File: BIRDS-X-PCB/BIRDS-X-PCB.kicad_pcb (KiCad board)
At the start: 2 copper layers, 85 x 85 mm, 84 parts, among them J101 LPC-50M2LG, J102 Conn_02x04_Odd_Even, J201 Conn_01x02, J202 Conn_01x02, J203 Conn_01x02, J401 Conn_01x04, J402 Conn_01x08, J403 Conn_01x02, J404 MHDR2X5, Q201 SI1470DH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

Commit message: PCB updated
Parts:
- moved U307 48.3 mm to (95.2, 97.5)
- moved R301 47.1 mm to (101.0, 97.0), turned to 90 degrees
- moved TP301 35.6 mm to (56.2, 68.0)
- moved JP301 19.5 mm to (87.0, 53.8)
- moved TP401 4.51 mm to (56.2, 72.0)
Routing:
- net Net-(U304-DIODE_ANODE): track 0.00 -> 103.8 mm
- net BOOT0: track 6.35 -> 103.2 mm, vias 0 -> 8
- net UART_TX_JASPER_TO_BOSS: track 0.00 -> 86.3 mm, vias 0 -> 2
- net TEMP_SENSE_1: track 0.00 -> 82.5 mm, vias 0 -> 4
- net ST_SWDIO: track 0.00 -> 82.5 mm, vias 0 -> 7
- net UART_RX_BOSS_TO_JASPER: track 0.00 -> 80.8 mm, vias 0 -> 2
- net Net-(U303-DIODE_ANODE): track 0.00 -> 77.6 mm, vias 0 -> 3
- net ST_RST: track 16.1 -> 86.3 mm, vias 2 -> 5
- net Net-(U301-DIODE_ANODE): track 0.00 -> 52.0 mm, vias 0 -> 2
- net DIO1_3V3_EN_FROM_BOSS: track 3.49 -> 50.0 mm, vias 0 -> 3
- net Net-(D301-K): track 0.00 -> 44.8 mm, vias 0 -> 3
- net Net-(U401-PA11/PA9): track 0.00 -> 41.4 mm, vias 0 -> 2
- net Net-(U302-DIODE_ANODE): track 0.00 -> 39.0 mm, vias 0 -> 2
- net SUP_3V3_2: track 7.48 -> 45.9 mm, vias 0 -> 1
- net Net-(JP301-B): track 0.00 -> 34.0 mm, vias 0 -> 2
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
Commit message: Fix DRC issues
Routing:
- net Net-(J402-Pin_7): track 5.62 -> 46.4 mm, vias 0 -> 4
- net GND: track 2.54 -> 26.9 mm, vias 0 -> 24
- net Net-(J402-Pin_3): track 4.12 -> 23.7 mm, vias 0 -> 3
- net ST_RST: track 86.3 -> 90.5 mm, vias 5 -> 6
- net Net-(U305A--): track 0.00 -> 3.31 mm
- net Net-(U305B--): track 0.00 -> 3.25 mm
- net Net-(U302-DIODE_ANODE): track 39.0 -> 36.0 mm
- net SUP_UNREG_2: track 0.00 -> 2.00 mm
- net SUP_3V3_1: track 0.00 -> 2.00 mm
- net BOOT0: track 103.2 -> 101.4 mm, vias 8 -> 6
- net SUP_5V0: track 33.3 -> 31.8 mm
- net RFET_EN3: track 76.3 -> 74.9 mm, vias 5 -> 4
- net SUP_3V3_2: track 45.9 -> 44.8 mm
- net DIO1_3V3_EN_FROM_BOSS: track 50.0 -> 48.9 mm
- net +5V: track 82.6 -> 81.7 mm
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
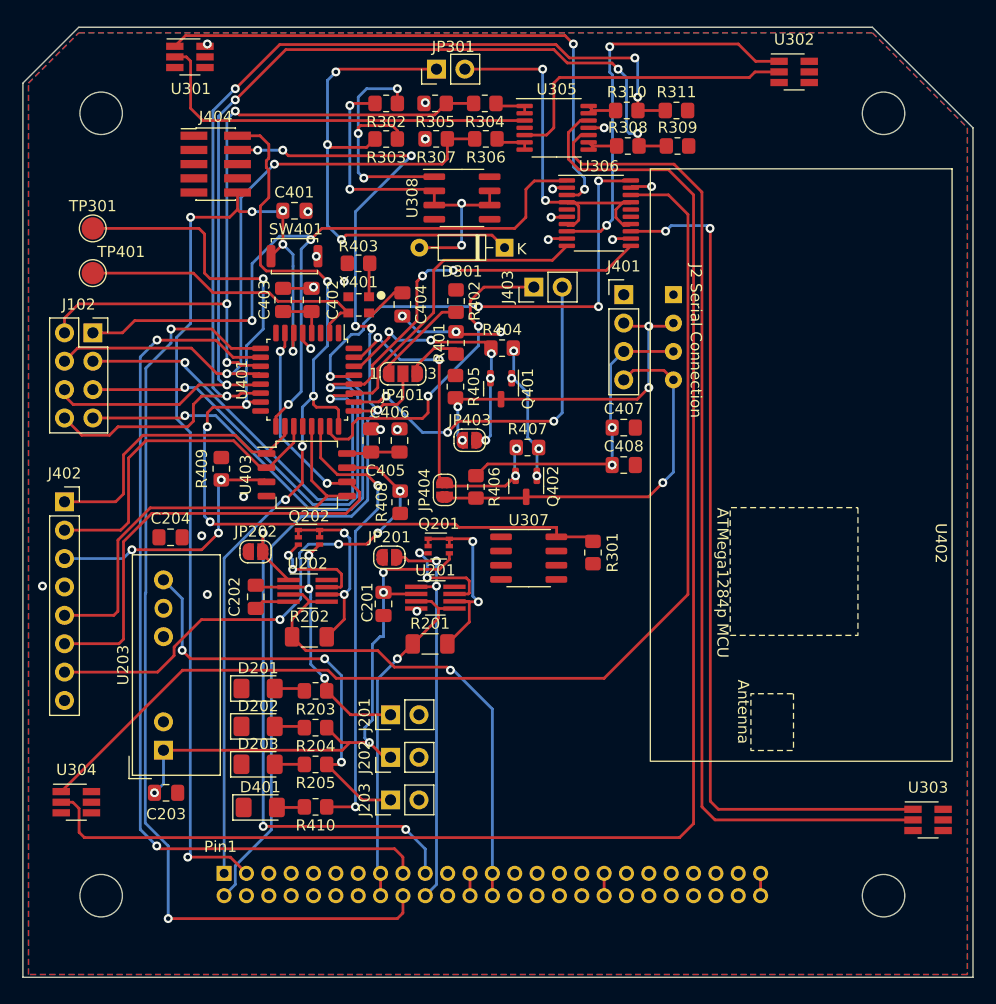
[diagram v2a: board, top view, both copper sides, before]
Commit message: Finish fixing DRC issues, except power lines
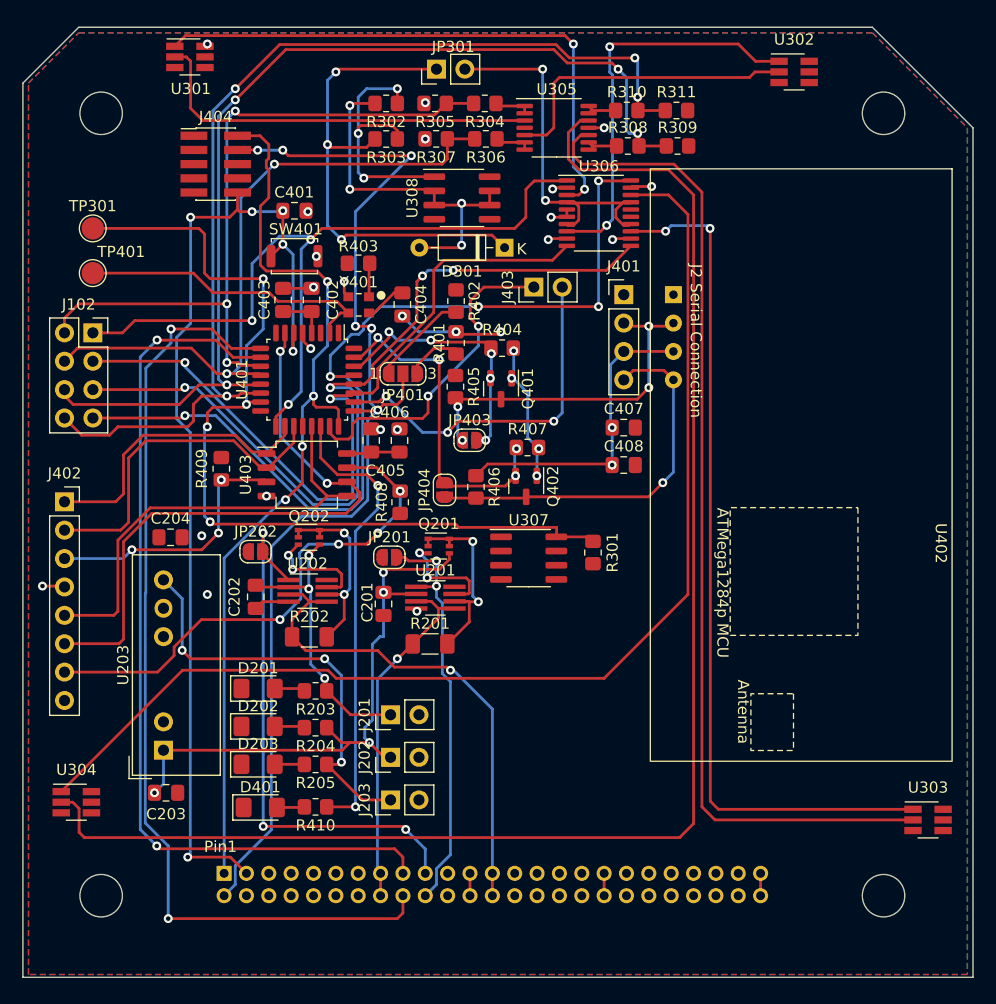
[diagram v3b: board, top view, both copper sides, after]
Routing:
- net GND: track 26.9 -> 31.0 mm
- net DIO2_5V_EN_FROM_BOSS: track 35.9 -> 36.9 mm
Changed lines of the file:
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@@
       (net 20 "SUP_5V0") (pinfunction "GATEP") (pintype "output"))
     (pad "4" smd rect (at -1.71 0.97) (size 2 0.4) (layers "F.Cu" "F.Paste" "F.Mask")
-      (net 2 "GND") (pinfunction "GND") (pintype "power_in"))
+      (net 2 "GND") (pinfunction "GND") (pintype "power_in") (zone_connect 2))
     (pad "5" smd rect (at 1.71 0.97) (size 2 0.4) (layers "F.Cu" "F.Paste" "F.Mask")
       (net 20 "SUP_5V0") (pinfunction "IN") (pintype "input"))
@@
       (net 28 "SUP_3V3_2") (pinfunction "GATEP") (pintype "output"))
     (pad "4" smd rect (at -1.71 0.97) (size 2 0.4) (layers "F.Cu" "F.Paste" "F.Mask")
-      (net 2 "GND") (pinfunction "GND") (pintype "power_in"))
+      (net 2 "GND") (pinfunction "GND") (pintype "power_in") (zone_connect 2))
     (pad "5" smd rect (at 1.71 0.97) (size 2 0.4) (layers "F.Cu" "F.Paste" "F.Mask")
       (net 28 "SUP_3V3_2") (pinfunction "IN") (pintype "input"))
@@
       (net 2 "GND") (pinfunction "GND") (pintype "power_in"))
     (pad "5" thru_hole oval (at 10.16 0 90) (size 1.7 1.7) (drill 1) (layers "*.Cu" "*.Mask")
-      (net 2 "GND") (pinfunction "0V/-Vo") (pintype "power_out"))
+      (net 2 "GND") (pinfunction "0V/-Vo") (pintype "power_out") (zone_connect 2))
     (pad "6" thru_hole oval (at 12.7 0 90) (size 1.7 1.6) (drill 1) (layers "*.Cu" "*.Mask")
       (net 83 "unconnected-(U203-NC{slash}0V-Pad6)") (pinfunction "NC/0V") (pintype "power_out+no_connect"))
@@
       (net 4 "+12V") (pinfunction "Pin_1") (pintype "passive"))
     (pad "2" thru_hole oval (at 0 2.54 90) (size 1.7 1.7) (drill 1) (layers "*.Cu" "*.Mask")
-      (net 2 "GND") (pinfunction "Pin_2") (pintype "passive"))
+      (net 2 "GND") (pinfunction "Pin_2") (pintype "passive") (zone_connect 2))
     (model "${KICAD6_3DMODEL_DIR}/Connector_PinHeader_2.54mm.3dshapes/PinHeader_1x02_P2.54mm_Vertical.wrl"
       (offset (xyz 0 0 0))
@@
       (net 126 "Net-(JP301-B)") (pintype "passive"))
     (pad "5" smd roundrect (at -2.8625 -0.325) (size 1.475 0.4) (layers "F.Cu" "F.Paste" "F.Mask") (roundrect_rratio 0.25)
-      (net 2 "GND") (pinfunction "VSS") (pintype "power_in"))
+      (net 2 "GND") (pinfunction "VSS") (pintype "power_in") (zone_connect 2))
     (pad "6" smd roundrect (at -2.8625 0.325) (size 1.475 0.4) (layers "F.Cu" "F.Paste" "F.Mask") (roundrect_rratio 0.25)
       (net 2 "GND") (pinfunction "GND") (pintype "power_in"))
@@
       (net 19 "unconnected-(J101-Pin_12-Pad12)") (pinfunction "Pin_12") (pintype "passive+no_connect"))
     (pad "13" thru_hole oval locked (at 0 -12 270) (size 1.35 1.35) (drill 0.8) (layers "*.Cu" "*.Mask")
-      (net 2 "GND") (pinfunction "Pin_13") (pintype "passive"))
+      (net 2 "GND") (pinfunction "Pin_13") (pintype "passive") (zone_connect 2))
     (pad "14" thru_hole oval locked (at 2 -12 270) (size 1.35 1.35) (drill 0.8) (layers "*.Cu" "*.Mask")
-      (net 2 "GND") (pinfunction "Pin_14") (pintype "passive"))
+      (net 2 "GND") (pinfunction "Pin_14") (pintype "passive") (zone_connect 2))
     (pad "15" thru_hole oval locked (at 0 -14 270) (size 1.35 1.35) (drill 0.8) (layers "*.Cu" "*.Mask")
       (net 20 "SUP_5V0") (pinfunction "Pin_15") (pintype "passive"))
@@
   (segment (start 81.949695 104.525) (end 82.26 104.525) (width 0.25) (layer "B.Cu") (net 1))
   (segment (start 62.575 117.69) (end 61.77 118.495) (width 0.25) (layer "B.Cu") (net 1))
+  (segment (start 78.75 72.75) (end 78.75 73.744) (width 0.25) (layer "F.Cu") (net 2))
+  (segment (start 51.75 100) (end 53.645 100) (width 0.25) (layer "F.Cu") (net 2))
   (segment (start 88.975 77.475) (end 88.75 77.25) (width 0.25) (layer "F.Cu") (net 2))
+  (segment (start 78.75 73.744) (end 79.121 74.115) (width 0.25) (layer "F.Cu") (net 2))
   (segment (start 75.932 73.363) (end 75.819 73.363) (width 0.25) (layer "F.Cu") (net 2))
   (segment (start 97.09 68.91) (end 97 69) (width 0.25) (layer "F.Cu") (net 2))
@@
   (segment (start 92.75 77.25) (end 92.525 77.475) (width 0.25) (layer "F.Cu") (net 2))
   (segment (start 97.25 67) (end 98.625 67) (width 0.25) (layer "F.Cu") (net 2))
+  (segment (start 53.645 100) (end 53.721 100.076) (width 0.25) (layer "F.Cu") (net 2))
   (segment (start 106.25 64.25) (end 104.5 64.25) (width 0.25) (layer "F.Cu") (net 2))
   (segment (start 97.5045 64.36) (end 98.665 64.36) (width 0.25) (layer "F.Cu") (net 2))
@@
   (segment (start 71.435 101.395) (end 73.76 101.395) (width 0.25) (layer "F.Cu") (net 2))
   (segment (start 102.84 68.91) (end 102.75 69) (width 0.25) (layer "F.Cu") (net 2))
+  (segment (start 98.665 66.31) (end 98.665 66.96) (width 0.25) (layer "F.Cu") (net 2))
   (segment (start 70.83 102) (end 71.435 101.395) (width 0.25) (layer "F.Cu") (net 2))
   (segment (start 102 59) (end 100.6125 59) (width 0.25) (layer "F.Cu") (net 2))
@@
   (via (at 88.75 77.25) (size 0.8) (drill 0.4) (layers "F.Cu" "B.Cu") (net 2))
   (via (at 76 73.25) (size 0.8) (drill 0.4) (layers "F.Cu" "B.Cu") (net 2))
-  (via (at 69.75 92) (size 0.8) (drill 0.4) (layers "F.Cu" "B.Cu") (free) (net 2))
+  (via (at 71.794 91.948) (size 0.8) (drill 0.4) (layers "F.Cu" "B.Cu") (free) (net 2))
   (via (at 97.39 64.4745) (size 0.8) (drill 0.4) (layers "F.Cu" "B.Cu") (free) (net 2))
   (via (at 83.947 75.8405) (size 0.8) (drill 0.4) (layers "F.Cu" "B.Cu") (net 2))
@@
   (via (at 87 97.75) (size 0.8) (drill 0.4) (layers "F.Cu" "B.Cu") (net 24))
   (via (at 87 100) (size 0.8) (drill 0.4) (layers "F.Cu" "B.Cu") (net 24))
-  (segment (start 87 100) (end 87 126.7) (width 0.25) (layer "B.Cu") (net 24))
-  (segment (start 87 126.7) (end 86 127.7) (width 0.25) (layer "B.Cu") (net 24))
+  (segment (start 87.525 107.825805) (end 88.25 108.550805) (width 0.25) (layer "B.Cu") (net 24))
+  (segment (start 87 101) (end 87.525 101.525) (width 0.25) (layer "B.Cu") (net 24))
+  (segment (start 87 125.285786) (end 87 126.7) (width 0.25) (layer "B.Cu") (net 24))
+  (segment (start 87.525 101.525) (end 87.525 107.825805) (width 0.25) (layer "B.Cu") (net 24))
+  (segment (start 88.25 108.550805) (end 88.25 124.035786) (width 0.25) (layer "B.Cu") (net 24))
+  (segment (start 87 100) (end 87 101) (width 0.25) (layer "B.Cu") (net 24))
   (segment (start 87 97.75) (end 87 100) (width 0.25) (layer "B.Cu") (net 24))
+  (segment (start 87 126.7) (end 86 127.7) (width 0.25) (layer "B.Cu") (net 24))
+  (segment (start 88.25 124.035786) (end 87 125.285786) (width 0.25) (layer "B.Cu") (net 24))
   (segment (start 90 127.7) (end 90 125.7) (width 0.25) (layer "F.Cu") (net 27))
   (segment (start 88.25 107.5255) (end 87.9745 107.25) (width 0.25) (layer "F.Cu") (net 28))

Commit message: Route power lines on 2-layer board, if desired
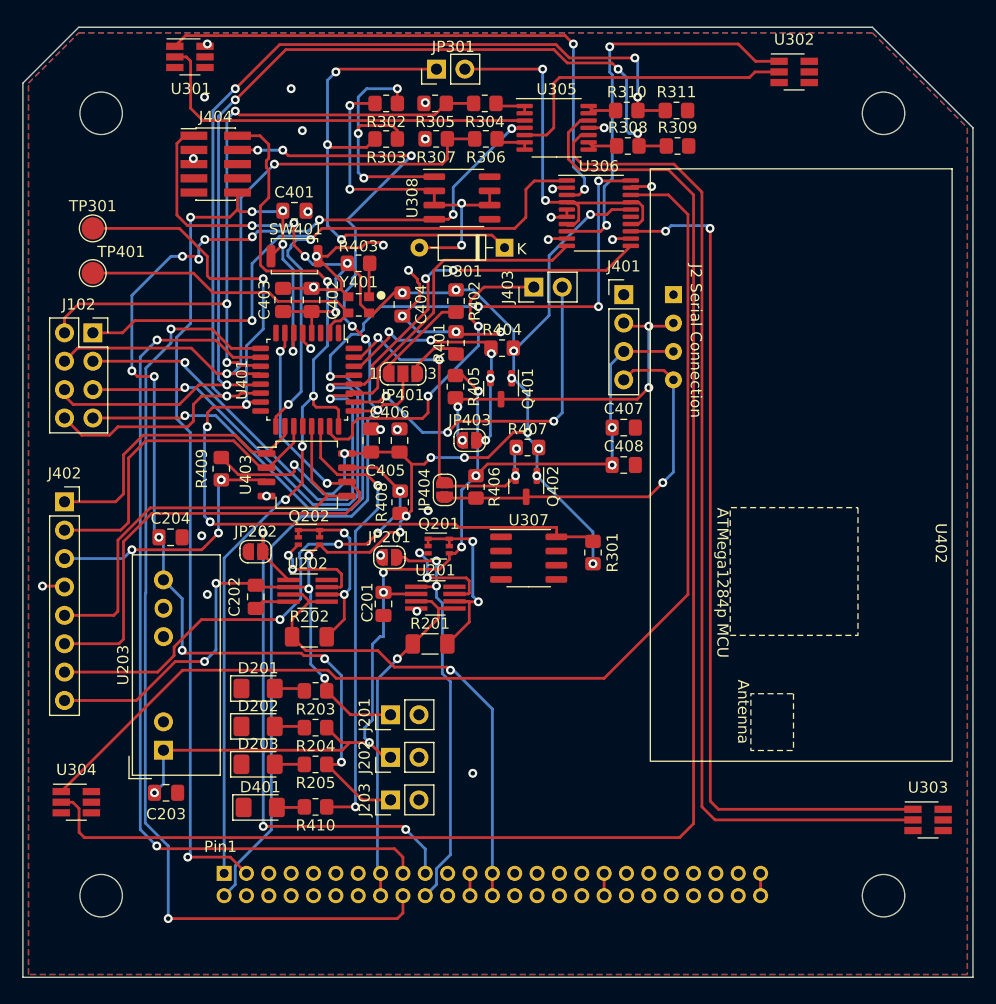
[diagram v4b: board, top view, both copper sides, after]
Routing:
- net +3V3: track 51.2 -> 201.8 mm, vias 7 -> 25
- net +12V: track 38.4 -> 109.6 mm, vias 3 -> 13
- net +5V: track 81.7 -> 100.2 mm, vias 6 -> 9
- net GND: track 31.0 -> 48.5 mm, vias 24 -> 32
- net RFET_EN1: track 70.7 -> 72.5 mm
- net TEMP_SENSE_1: track 81.8 -> 80.7 mm
- net BOOT0: track 101.4 -> 102.0 mm

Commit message: Minor layout changes to consolodate ground planes
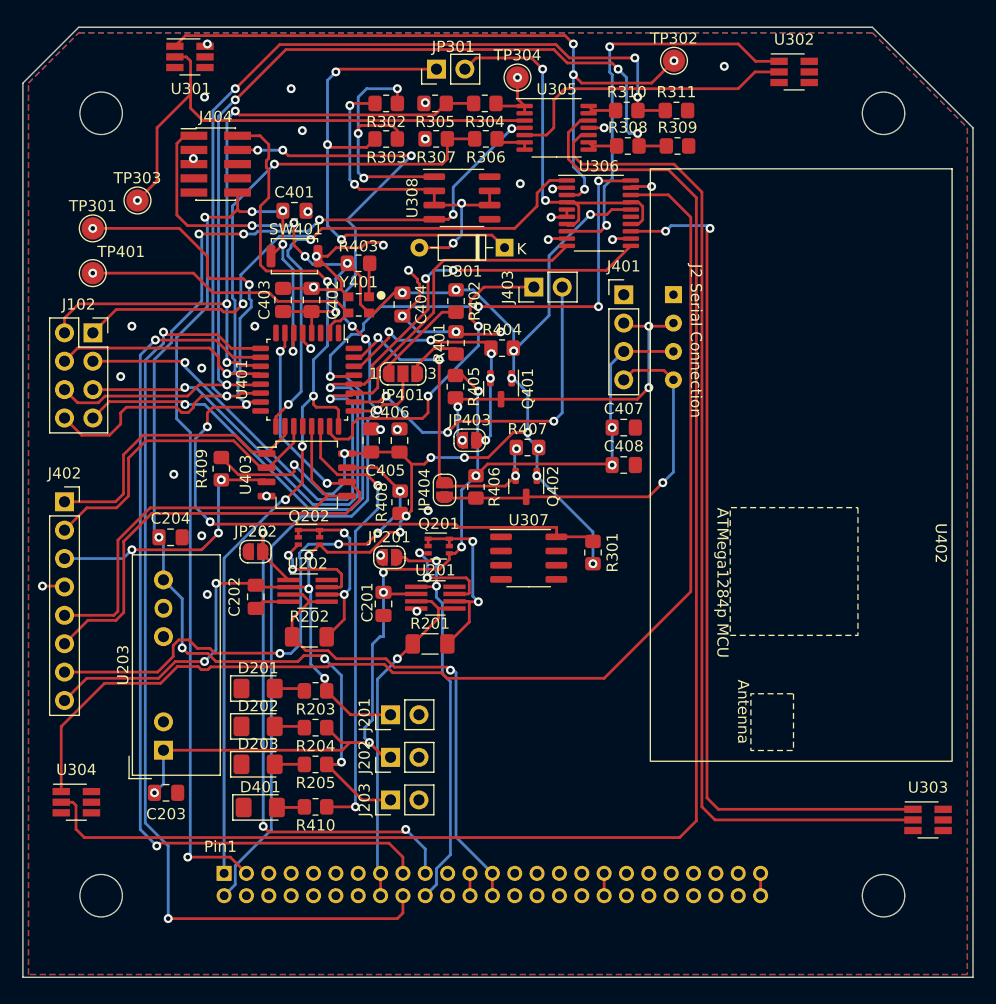
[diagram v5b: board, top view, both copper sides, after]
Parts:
- added TP302: TestPoint, TestPoint:TestPoint_Pad_D2.0mm, F.Cu at (108.2, 53.0)
- added TP303: TestPoint, TestPoint:TestPoint_Pad_D2.0mm, F.Cu at (60.2, 65.5)
- added TP304: TestPoint, TestPoint:TestPoint_Pad_D2.0mm, F.Cu at (94.2, 54.5)
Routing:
- net Net-(U301-SOURCE_BULK): track 36.1 -> 47.6 mm, vias 0 -> 1
- net Net-(U301-DIODE_ANODE): track 51.6 -> 61.7 mm, vias 2 -> 4
- net Net-(U304-DIODE_ANODE): track 103.8 -> 108.1 mm
- net Net-(J402-Pin_7): track 46.4 -> 49.9 mm
- net +12V: track 109.6 -> 106.3 mm, vias 13 -> 9
- net Net-(U305A--): track 3.31 -> 6.12 mm, vias 0 -> 1
- net RFET_EN1: track 72.5 -> 70.7 mm
- net MEM_MISO: track 30.6 -> 29.2 mm
- net MEM_CLK: track 56.2 -> 54.9 mm
- net Net-(D301-A): track 32.7 -> 31.6 mm
- net RFET_EN4: track 85.3 -> 86.4 mm
- net Net-(U302-SOURCE_BULK): track 27.4 -> 26.6 mm
- net Net-(JP301-B): track 33.8 -> 34.7 mm
- net RFET_OUT2: track 59.7 -> 60.4 mm
- net TEMP_SENSE_1: track 80.7 -> 80.1 mm, vias 4 -> 5
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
